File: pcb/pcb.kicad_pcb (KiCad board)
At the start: 2 copper layers, 6 parts, among them CON1 BARREL_JACK, P1 CONN_02X20, P2 CONN_01X04, U1 POLOLU_A4988

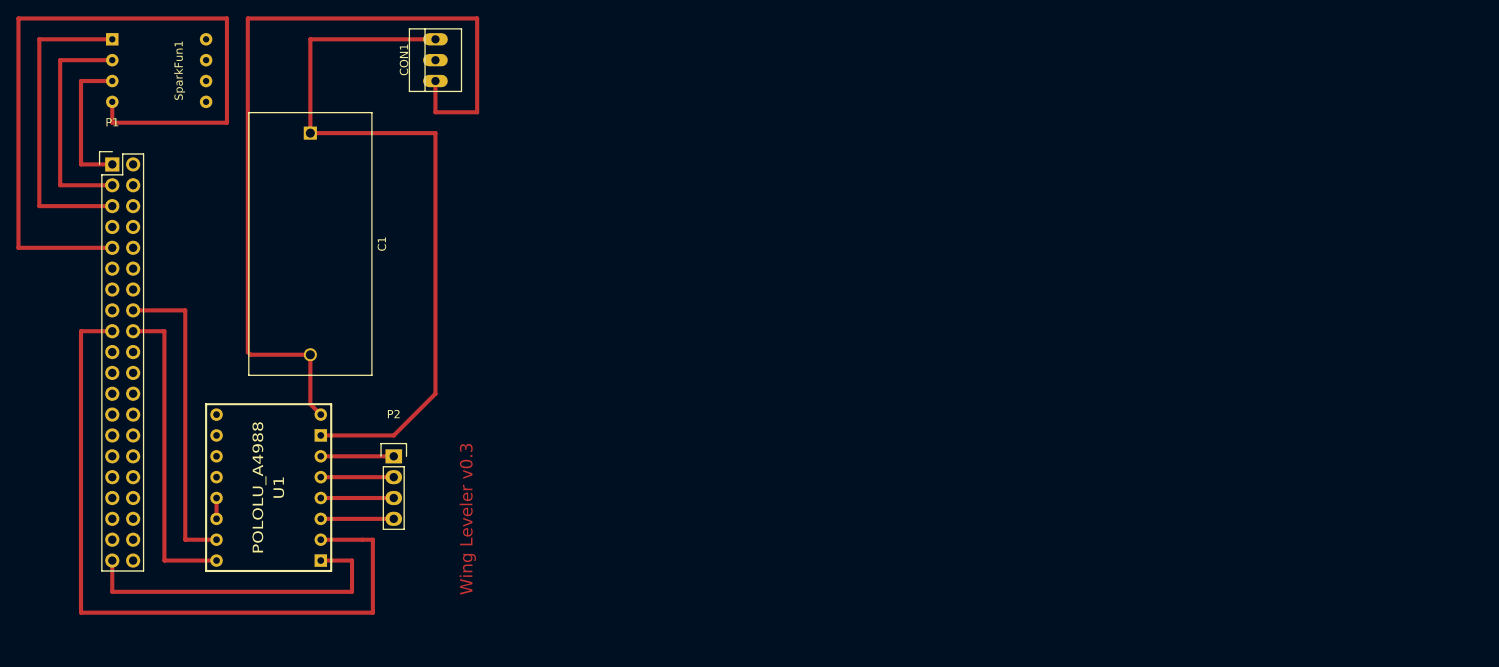
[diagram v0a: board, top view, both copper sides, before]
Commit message: fitting all the components on the pi top
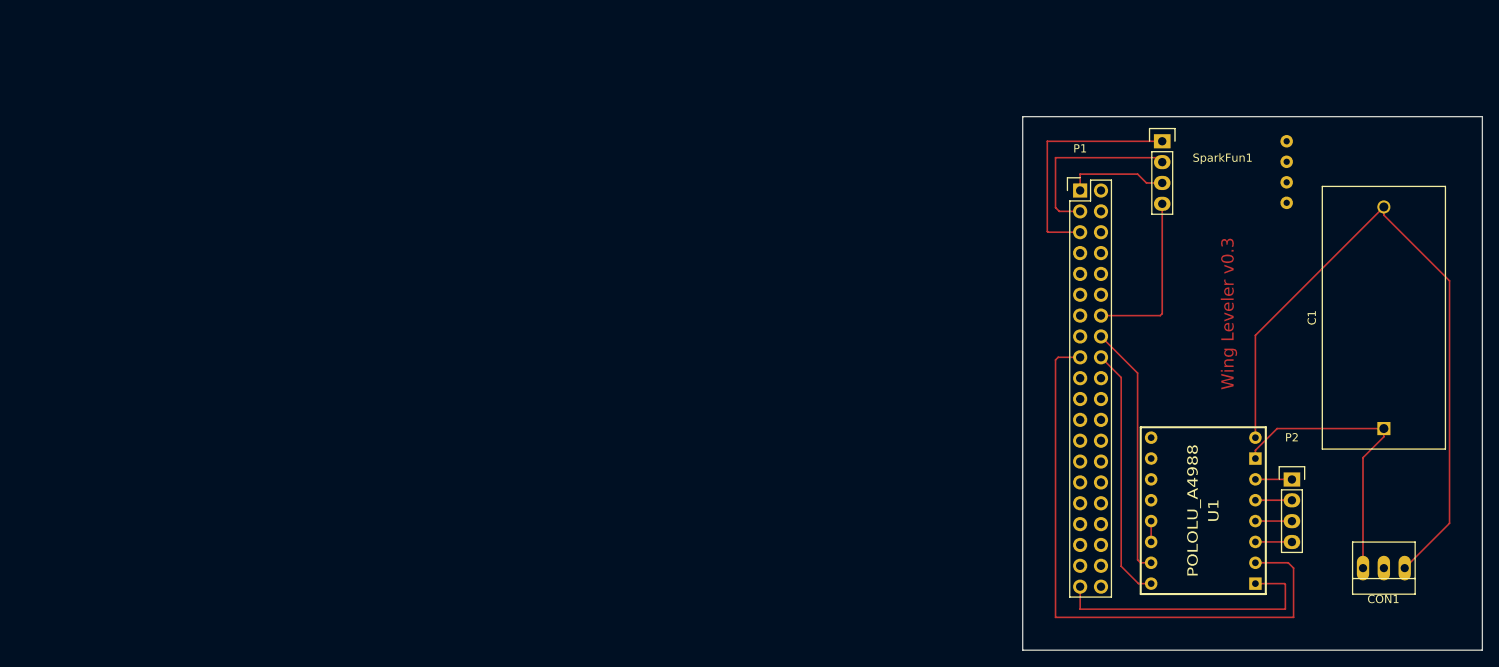
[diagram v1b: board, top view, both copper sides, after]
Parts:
- SparkFun1: footprint pololu:MPU9250 -> Connectors_Harwin:mpu9250SparkFun2
- moved SparkFun1 138.3 mm to (213.0, 81.0), turned to 0 degrees
- moved C1 135.6 mm to (240.0, 116.0), turned to 90 degrees
- moved CON1 131.1 mm to (240.0, 133.0), turned to 180 degrees
- moved P1 118.0 mm to (203.0, 87.0)
- moved U1 113.9 mm to (218.0, 126.0)
- moved P2 109.5 mm to (228.8, 122.2)
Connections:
- P1 pad 14: (no net) -> Net-(P1-Pad14)
- P1 pad 9: Net-(P1-Pad9) -> (no net)
- SparkFun1 pad 4: Net-(P1-Pad9) -> Net-(P1-Pad14)
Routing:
- net Net-(P1-Pad9): track 94.0 -> 0.00 mm
- net Net-(C1-Pad1): track 89.7 -> 35.8 mm
- net Net-(P1-Pad14): track 0.00 -> 20.9 mm
- net Net-(C1-Pad2): track 104.5 -> 84.2 mm
- net Net-(P1-Pad17): track 88.9 -> 74.4 mm
- net Net-(P1-Pad5): track 38.1 -> 29.0 mm
- net Net-(P1-Pad16): track 38.1 -> 30.9 mm
- net Net-(P1-Pad18): track 38.1 -> 31.0 mm
- net Net-(P1-Pad39): track 40.6 -> 34.4 mm
- net Net-(P1-Pad3): track 27.9 -> 22.5 mm
- net Net-(P1-Pad1): track 17.8 -> 12.4 mm
- net Net-(P2-Pad4): track 8.89 -> 4.45 mm
- net Net-(P2-Pad2): track 8.89 -> 4.45 mm
- net Net-(P2-Pad3): track 8.89 -> 4.45 mm
- net Net-(P2-Pad1): track 8.89 -> 4.45 mm
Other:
- board outline added: 56 x 65 mm
- net class Default: trace_width 0.5 -> 0.2
